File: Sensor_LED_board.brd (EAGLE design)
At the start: 114.3 x 25.4 mm, 22 parts, among them T1 2N2222

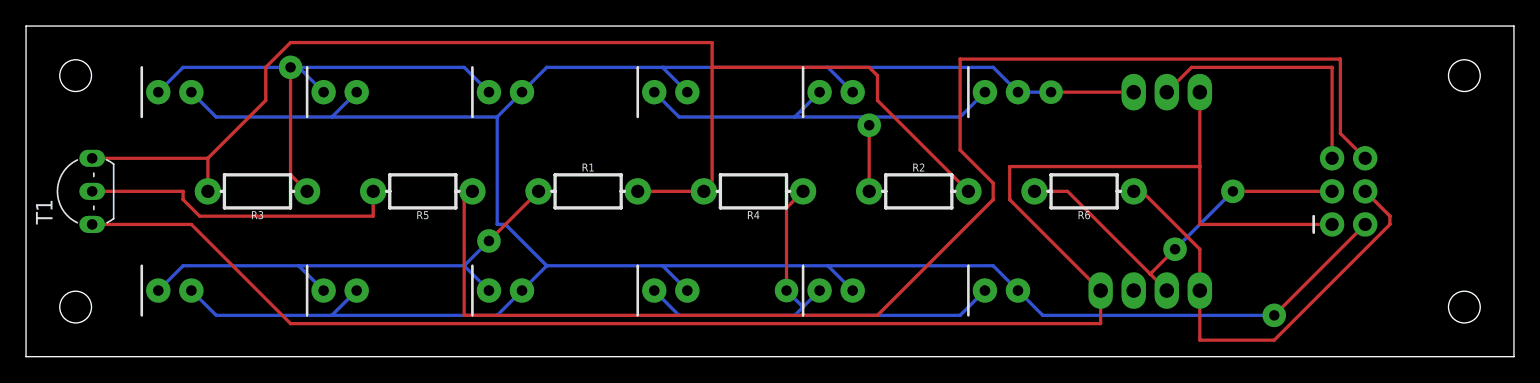
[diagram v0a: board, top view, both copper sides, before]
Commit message: Change DRC to 1/64
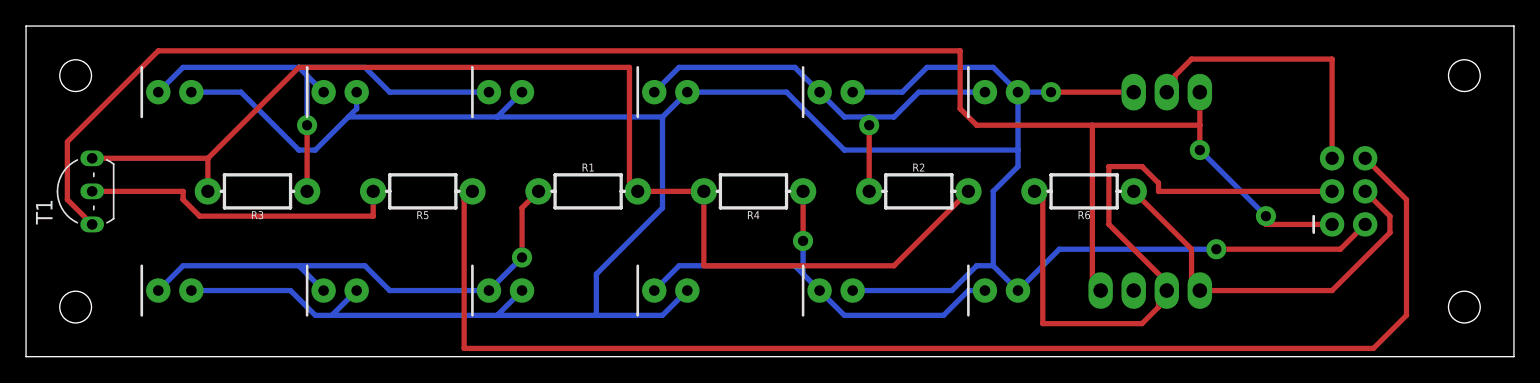
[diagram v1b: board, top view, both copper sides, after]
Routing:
- net PIN4: track 29.9 -> 51.0 mm, vias 2 -> 0
- net 5V: track 202.1 -> 216.6 mm
- net N$6: track 96.9 -> 90.0 mm
- net 3.3V: track 35.5 -> 30.1 mm
- net N$5: track 39.6 -> 34.9 mm
- net PIN19: track 103.6 -> 99.2 mm
- net GND: track 130.5 -> 132.3 mm, vias 0 -> 2
- net PIN17: track 20.5 -> 21.7 mm
- net N$3: track 39.7 -> 38.6 mm
- net N$2: track 35.4 -> 34.3 mm
- net N$1: track 37.8 -> 38.9 mm

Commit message: Put LED resistors in series, not parallel.
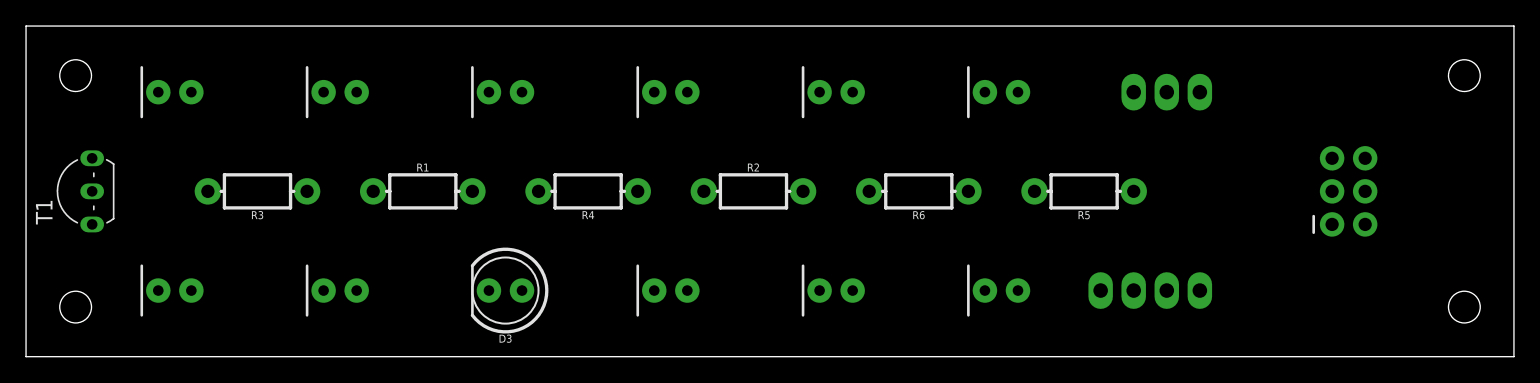
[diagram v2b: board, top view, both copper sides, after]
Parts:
- moved R5 50.8 mm to (81.3, 12.7)
- moved R4 12.7 mm to (43.2, 12.7)
- moved R6 12.7 mm to (68.6, 12.7)
- moved R1 12.7 mm to (30.5, 12.7)
- moved R2 12.7 mm to (55.9, 12.7)
- flipped D3 to the top, turned to 180 degrees
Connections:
- new net N$10: D8.K, D9.A
- new net N$11: D11.K, D12.A
- new net N$12: D6.K, R2.P$1
- new net N$13: D9.K, R3.P$1
- new net N$14: D12.K, R4.P$1
- new net N$7: D2.K, D3.A
- new net N$8: D3.K, R1.P$2
- new net N$9: D5.K, D6.A
- net 5V: no longer D11.A, D12.A, D2.A, D3.A, D5.A, D6.A, D8.A, D9.A
- net N$1: now also D2.A; no longer D2.K, D3.K, R1.P$1
- net N$2: now also D5.A; no longer D5.K, D6.K, R2.P$1
- net N$3: now also D8.A; no longer D8.K, D9.K, R3.P$1
- net N$5: now also D11.A; no longer D11.K, D12.K, R4.P$1
- net N$6: now also R1.P$1; no longer R1.P$2
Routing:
- net 5V: track 216.6 -> 0.00 mm, vias 2 -> 0
- net GND: track 132.3 -> 0.00 mm, vias 2 -> 0
- net PIN19: track 99.2 -> 0.00 mm
- net N$6: track 90.0 -> 0.00 mm
- net PIN4: track 51.0 -> 0.00 mm
- net N$1: track 38.9 -> 0.00 mm, vias 1 -> 0
- net N$3: track 38.6 -> 0.00 mm, vias 1 -> 0
- net N$5: track 34.9 -> 0.00 mm, vias 1 -> 0
- net N$2: track 34.3 -> 0.00 mm, vias 1 -> 0
- net 3.3V: track 30.1 -> 0.00 mm
- net N$4: track 24.7 -> 0.00 mm
- net PIN17: track 21.7 -> 0.00 mm

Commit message: Redo:  Put LED resistors in series, not parallel.
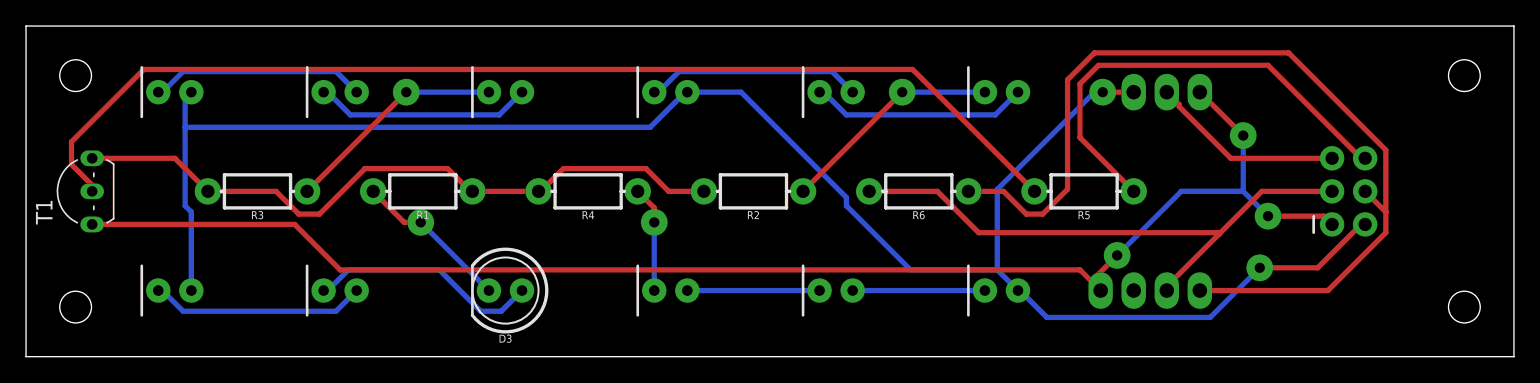
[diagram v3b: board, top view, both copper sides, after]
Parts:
- turned R1 to 180 degrees
- turned R2 to 180 degrees
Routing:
- net 5V: track 0.00 -> 137.7 mm, vias 0 -> 2
- net GND: track 0.00 -> 111.9 mm, vias 0 -> 3
- net N$4: track 0.00 -> 84.6 mm
- net 3.3V: track 0.00 -> 70.7 mm
- net N$6: track 0.00 -> 52.4 mm
- net PIN4: track 0.00 -> 44.3 mm
- net PIN19: track 0.00 -> 35.4 mm
- net N$7: track 0.00 -> 17.9 mm
- net N$13: track 0.00 -> 17.1 mm, vias 0 -> 1
- net N$12: track 0.00 -> 17.1 mm, vias 0 -> 1
- net N$9: track 0.00 -> 16.7 mm
- net N$10: track 0.00 -> 16.7 mm
- net N$2: track 0.00 -> 16.6 mm
- net N$3: track 0.00 -> 16.6 mm
- net N$1: track 0.00 -> 16.6 mm
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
